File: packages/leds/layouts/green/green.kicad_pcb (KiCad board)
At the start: 2 copper layers, 2 parts, among them U1 2.75V

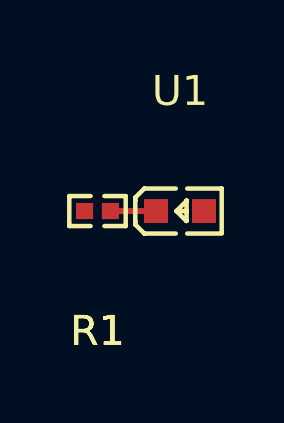
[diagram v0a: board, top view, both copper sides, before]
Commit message: rebuild all packages & regenerate images of changed layouts (silk)
Add new scripts for version bump and build (based on atopile/packages)
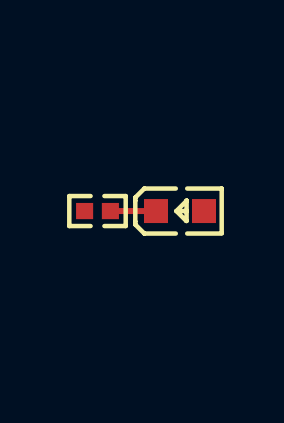
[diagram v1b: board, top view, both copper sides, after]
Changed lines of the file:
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@@
             (at 0 -4 0)
             (layer "F.SilkS")
-            (hide no)
+            (hide yes)
             (effects
                 (font
@@
                     (thickness 0.15)
                 )
+                (hide yes)
             )
             (unlocked no)
@@
                     (thickness 0.15)
                 )
+                (hide yes)
             )
             (unlocked no)
@@
             (at 0 -4 0)
             (layer "F.SilkS")
-            (hide no)
+            (hide yes)
             (effects
                 (font
@@
             )
         )
-        (property "checksum" "cc3916d01dbb7d14660eb363b35ab5feaf955d94c28cf00c8581ba5b0f81baad"
+        (property "checksum" "a88789bfdfa13149b5bde1802d94059948157b8125f31f42098ca4689dfb276e"
             (at 0 0 0)
             (layer "User.9")
@@
             )
         )
-        (property "__atopile_lib_fp_hash__" "ef18c490-9020-b315-071e-1cfc458608d0"
+        (property "__atopile_lib_fp_hash__" "4862f152-7716-38a8-1fce-05998a37525b"
             (at 0 0 0)
             (layer "User.9")
@@
                     (thickness 0.15)
                 )
+                (hide yes)
             )
             (unlocked no)
